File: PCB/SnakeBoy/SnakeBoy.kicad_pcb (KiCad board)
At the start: 2 copper layers, 15 parts, among them SW1 SW_Push, SW2 SW_Push, SW3 SW_Push, SW4 SW_Push, SW5 SW_Push, SW6 SW_Push, SW7 SW_DIP_x01, U1 ESP32-S3-DEVKITC-1-N16R8, U2 COM-09032, U3 PAM8304 Module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

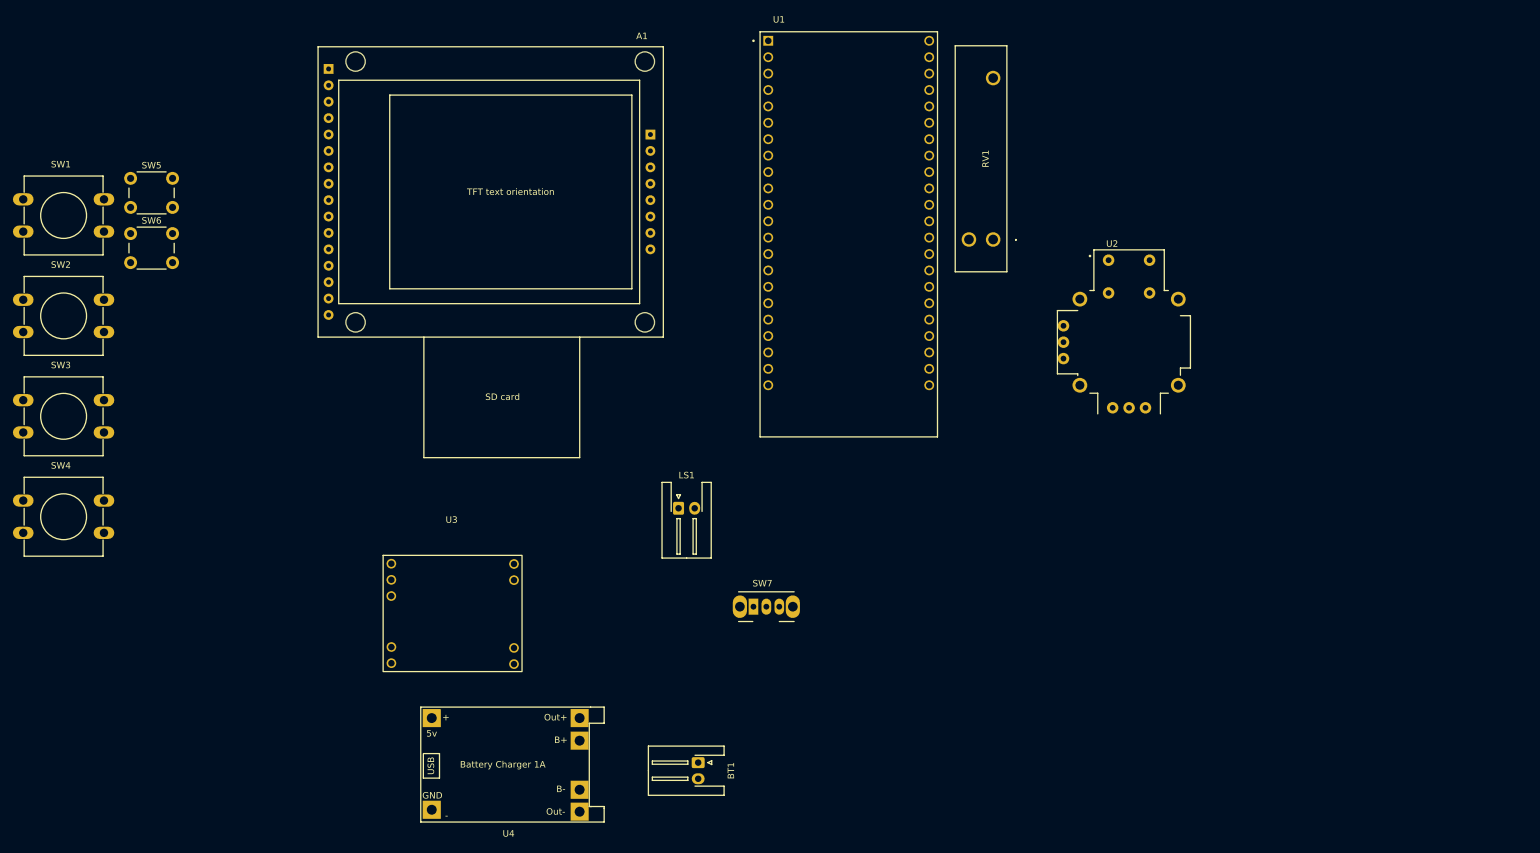
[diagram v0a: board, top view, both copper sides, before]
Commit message: Finished the Controller and Display schems
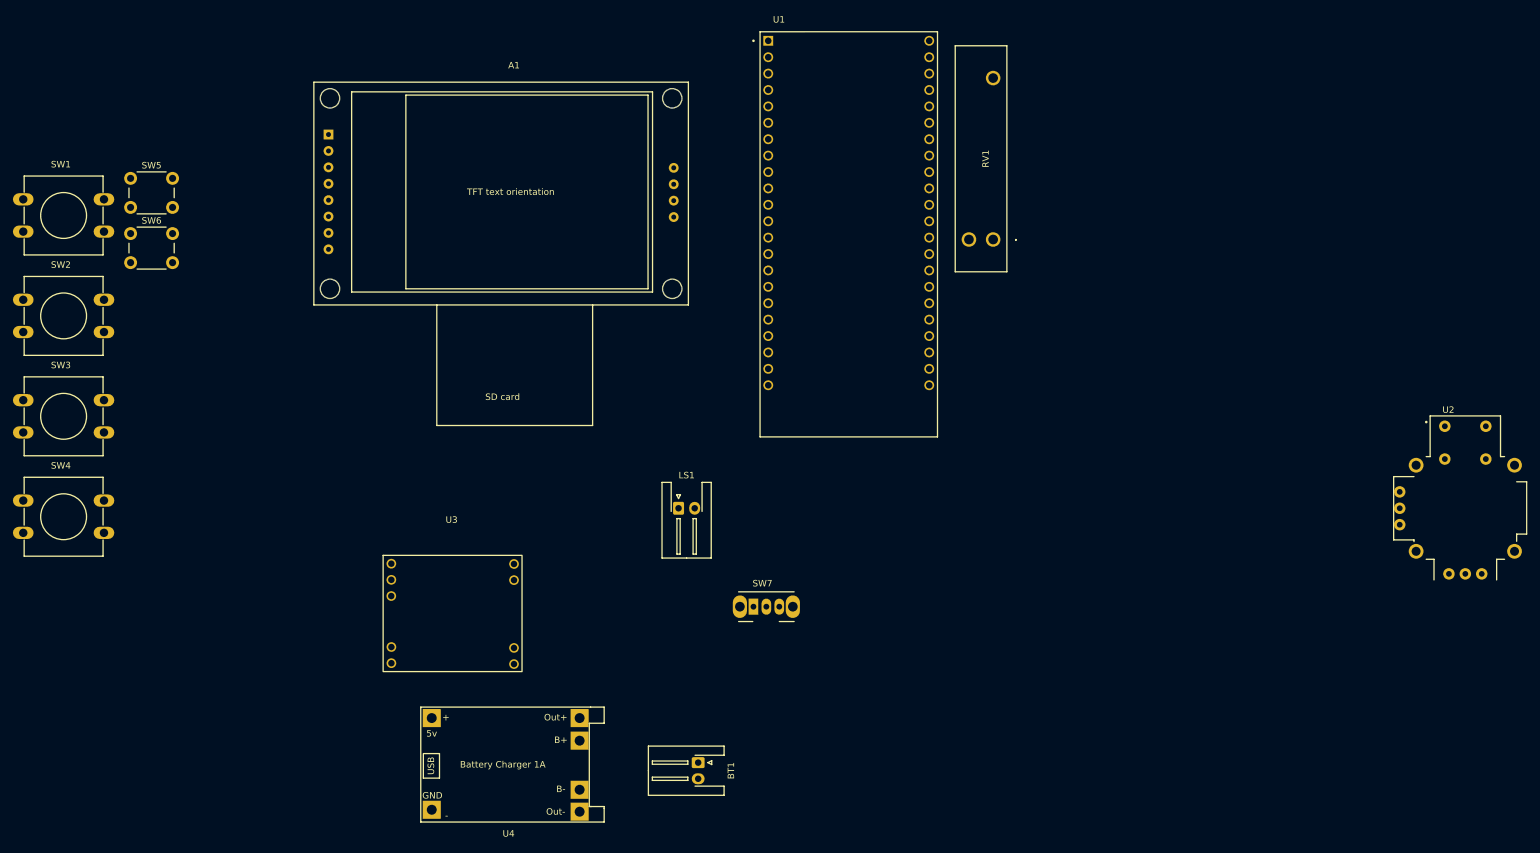
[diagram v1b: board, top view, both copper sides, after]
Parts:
- moved U2 58.1 mm to (275.6, 137.2)

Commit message: Finished the schematic
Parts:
- added LS2: Speaker, Connector_JST:JST_XH_S2B-XH-A-1_1x02_P2.50mm_Horizontal, F.Cu at (232.4, 69.3)
- added R1: 10Kohm, Resistor_THT:R_Axial_DIN0309_L9.0mm_D3.2mm_P12.70mm_Horizontal, F.Cu at (214.6, 66.8)
- added R2: 10Kohm, Resistor_THT:R_Axial_DIN0309_L9.0mm_D3.2mm_P12.70mm_Horizontal, F.Cu at (214.6, 71.5)
- added R3: 10Kohm, Resistor_THT:R_Axial_DIN0309_L9.0mm_D3.2mm_P12.70mm_Horizontal, F.Cu at (214.6, 76.2)
- added R4: 10Kohm, Resistor_THT:R_Axial_DIN0309_L9.0mm_D3.2mm_P12.70mm_Horizontal, F.Cu at (214.6, 81.0)
- added R5: 10Kohm, Resistor_THT:R_Axial_DIN0309_L9.0mm_D3.2mm_P12.70mm_Horizontal, F.Cu at (214.6, 85.8)
- added R6: 10Kohm, Resistor_THT:R_Axial_DIN0309_L9.0mm_D3.2mm_P12.70mm_Horizontal, F.Cu at (214.6, 90.5)
- added R7: 10Kohm, Resistor_THT:R_Axial_DIN0309_L9.0mm_D3.2mm_P12.70mm_Horizontal, F.Cu at (214.6, 95.2)
- A1: value TFT -> TFT 1.8 inch
- RV1: value 10Kohm_Potentiometer_Small -> R_Potentiometer_Dual; footprint slider:RA2043F2010EB1B10K -> slider:PS45M0MC2BR10KN
- SW1: value SW_Push -> X
- SW2: value SW_Push -> A
- SW3: value SW_Push -> Y
- SW4: value SW_Push -> B
- SW5: value SW_Push -> Start
- SW6: value SW_Push -> Select
- SW7: value SW_DIP_x01 -> Power_SW
- U2: value COM-09032 -> Joystick
- moved U2 21.6 mm to (256.5, 147.3), turned to -90 degrees
- moved RV1 8.62 mm to (201.9, 104.1)
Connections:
- A1 pad 13L: unconnected-(A1-SD_MOSI-Pad13L) -> SD_MOSI
- A1 pad 14L: unconnected-(A1-SD_~{CS}-Pad14L) -> SD_CS
- A1 pad 15L: unconnected-(A1-NC-Pad15L) -> (no net)
- A1 pad 16L: unconnected-(A1-NC-Pad16L) -> (no net)
- A1 pad 1R: unconnected-(A1-TFT_~{RST}-Pad1R) -> TFT_RST
- A1 pad 2R: unconnected-(A1-TFT_~{CS}-Pad2R) -> TFT_CS
- A1 pad 3R: unconnected-(A1-TFT_D~{C}-Pad3R) -> TFT_DC
- A1 pad 4R: unconnected-(A1-TFT_DIN-Pad4R) -> TFT_DIN
- A1 pad 5R: unconnected-(A1-TFT_CLK-Pad5R) -> TFT_CLK
- A1 pad 6R: unconnected-(A1-VCC-Pad6R) -> 3v7+
- A1 pad 7R: unconnected-(A1-TFT_BL-Pad7R) -> TFT_BL
- A1 pad 8R: unconnected-(A1-GND-Pad8R) -> 3v7-
- SW1 pad 1: unconnected-(SW1-Pad1) -> BT_X
- SW1 pad 2: unconnected-(SW1-Pad2) -> 3v7+
- SW2 pad 1: unconnected-(SW2-Pad1) -> BT_A
- SW2 pad 2: unconnected-(SW2-Pad2) -> 3v7+
- SW3 pad 1: unconnected-(SW3-Pad1) -> BT_Y
- SW3 pad 2: unconnected-(SW3-Pad2) -> 3v7+
- SW4 pad 1: unconnected-(SW4-Pad1) -> BT_B
- SW4 pad 2: unconnected-(SW4-Pad2) -> 3v7+
- SW5 pad 1: unconnected-(SW5-Pad1) -> BT_Start
- SW5 pad 2: unconnected-(SW5-Pad2) -> 3v7+
- SW6 pad 1: unconnected-(SW6-Pad1) -> BT_Select
- SW7 pad 1: unconnected-(SW7-Pad1) -> Net-(U4-OUT+)
- SW7 pad 2: unconnected-(SW7-Pad2) -> 3v7+
- U2 pad B1A: unconnected-(U2-SEL+-PadB1A) -> BT_joymid
- U2 pad B2A: unconnected-(U2-SEL--PadB2A) -> 3v7+
- U2 pad H1: unconnected-(U2-H+-PadH1) -> 3v7+
- U2 pad H2: unconnected-(U2-H-PadH2) -> Joy_X
- U2 pad H3: unconnected-(U2-H--PadH3) -> 3v7-
- U2 pad S1: Net-(U2-SHIELD-PadS1) -> 3v7-
- U2 pad S2: Net-(U2-SHIELD-PadS1) -> 3v7-
- U2 pad S3: Net-(U2-SHIELD-PadS1) -> 3v7-
- U2 pad S4: Net-(U2-SHIELD-PadS1) -> 3v7-
- U2 pad V1: unconnected-(U2-V+-PadV1) -> 3v7+
- U2 pad V2: unconnected-(U2-V-PadV2) -> Joy_Y
- U2 pad V3: unconnected-(U2-V--PadV3) -> 3v7-
- U3 pad 1: unconnected-(U3-5v+-Pad1) -> 3v7+
- U3 pad 2: unconnected-(U3-GND-Pad2) -> 3v7-
- U3 pad 4: unconnected-(U3-GND-Pad4) -> 3v7-
- U4 pad 1: unconnected-(U4-5V+-Pad1) -> +5V
- U4 pad 2: unconnected-(U4-GND-Pad2) -> GND
- U4 pad 3: unconnected-(U4-OUT+-Pad3) -> Net-(U4-OUT+)
- U4 pad 4: unconnected-(U4-OUT--Pad4) -> 3v7-

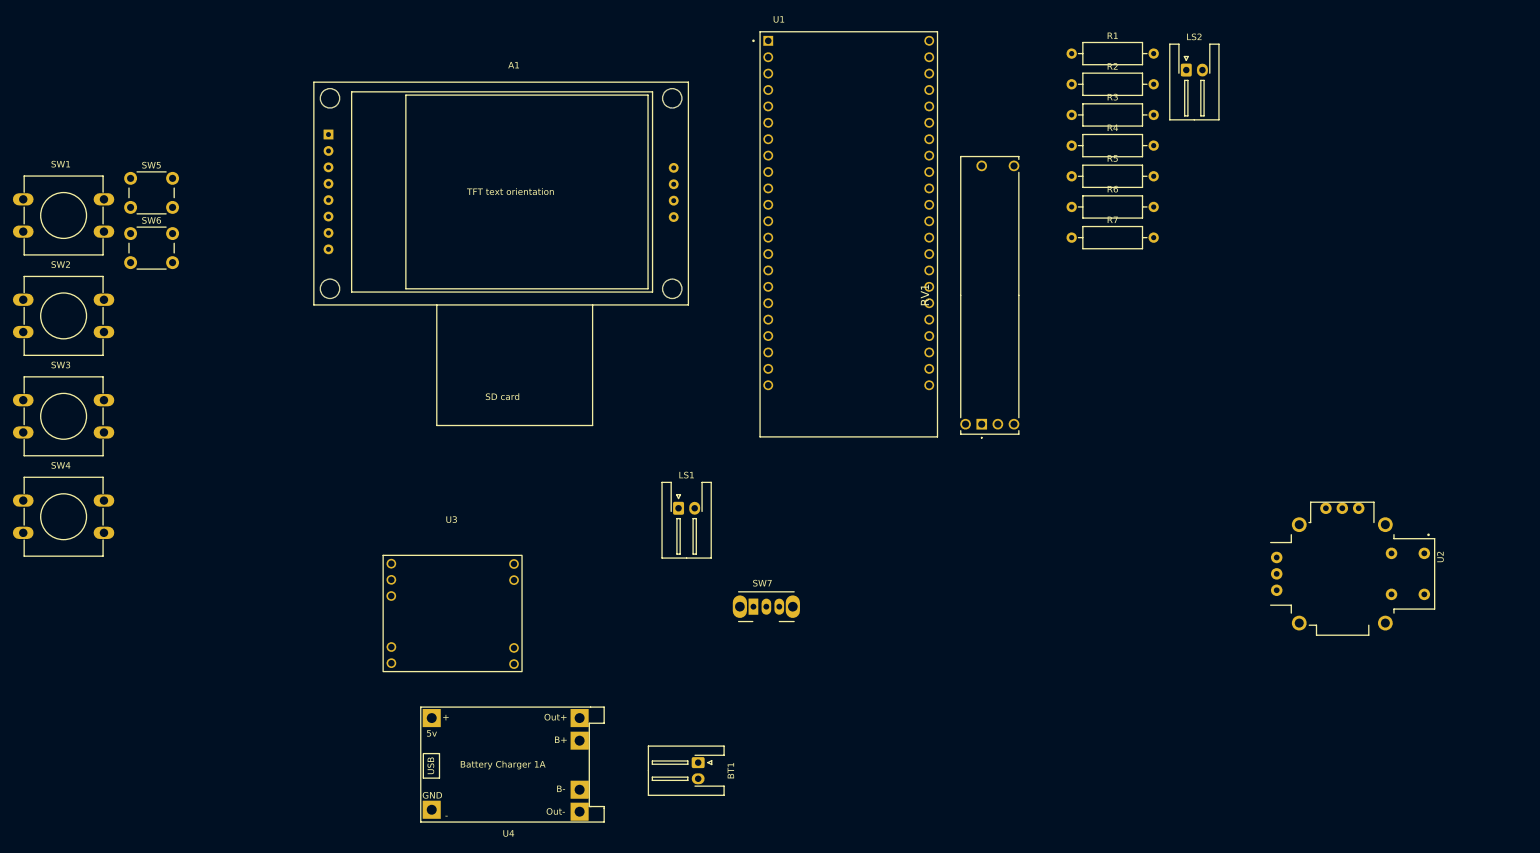
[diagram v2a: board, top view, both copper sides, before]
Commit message: Outlined the PCB
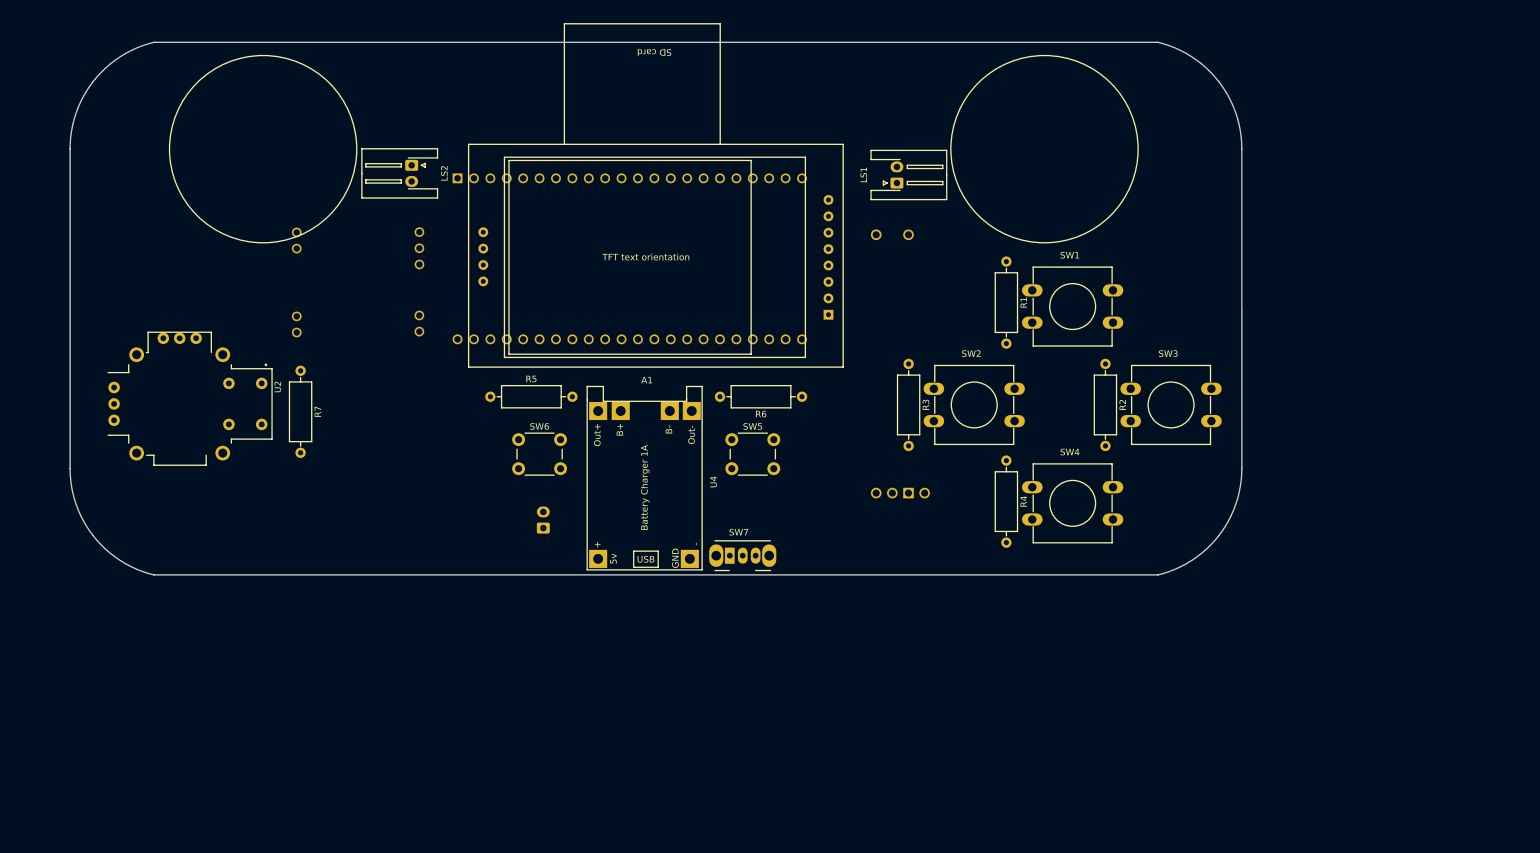
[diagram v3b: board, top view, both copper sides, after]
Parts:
- BT1, RV1, U1, U3: moved to B.Cu
- moved U2 182.0 mm to (76.5, 121.0)
- moved SW3 171.5 mm to (223.8, 118.7)
- moved SW1 156.9 mm to (208.5, 103.4)
- moved SW4 156.3 mm to (208.5, 133.9)
- moved SW2 141.7 mm to (193.3, 118.7)
- moved R7 121.2 mm to (95.2, 115.9), turned to -90 degrees
- moved LS2 120.9 mm to (112.4, 84.0), turned to -90 degrees
- moved SW5 101.5 mm to (162.0, 126.5)
- moved R5 96.3 mm to (124.6, 119.9)
- moved SW6 68.0 mm to (129.0, 126.5)
- moved LS1 60.7 mm to (187.6, 86.8), turned to 90 degrees
- moved U3 53.3 mm to (104.3, 102.1), turned to 180 degrees
- moved R6 51.1 mm to (172.9, 119.9), turned to 180 degrees
- moved R4 49.8 mm to (204.5, 129.8), turned to -90 degrees
- moved R3 46.1 mm to (189.4, 114.8), turned to -90 degrees
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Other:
- board outline added: 181.5 x 82.5 mm
